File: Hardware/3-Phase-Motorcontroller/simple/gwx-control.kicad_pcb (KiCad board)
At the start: 2 copper layers, 54 x 33 mm, 41 parts, among them IC1 74LS02D, IC2 74123D, J1 MTA07-100, T1 BC850, T2 BC850

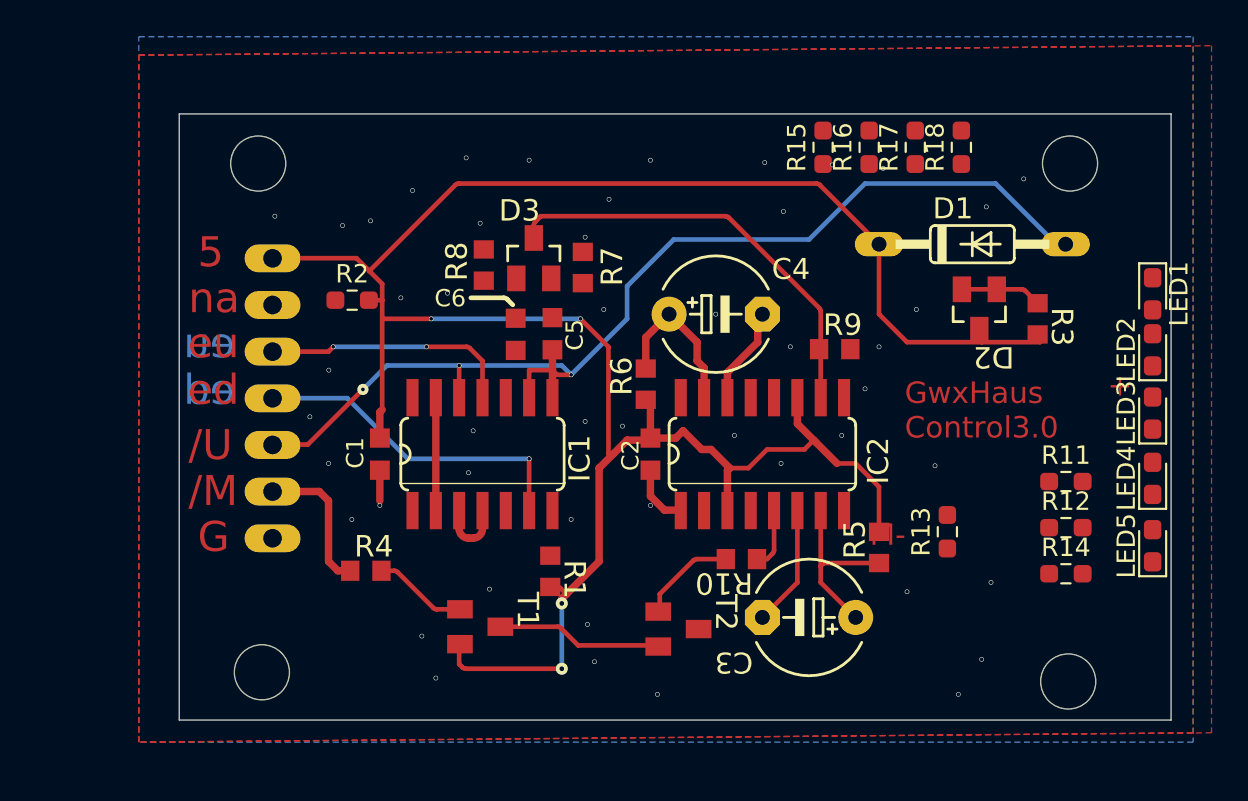
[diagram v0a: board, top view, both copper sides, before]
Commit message: Changed to 2x8 connector
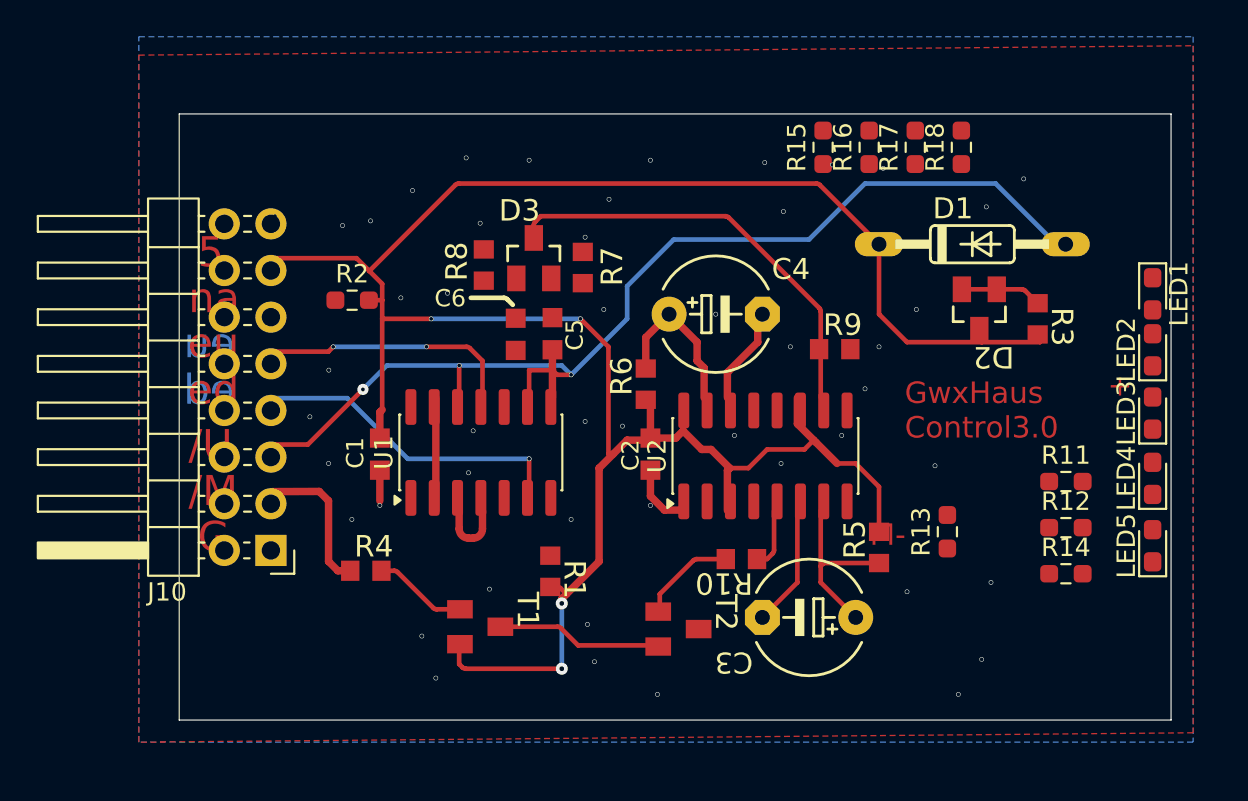
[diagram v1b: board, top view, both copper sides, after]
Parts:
- removed IC1: 74LS02D, SO14
- removed IC2: 74123D, SO16
- removed J1: MTA07-100, 10X07MTA
- removed UNK_HOLE_0: , dummyfp0
- removed UNK_HOLE_1: , dummyfp1
- removed UNK_HOLE_2: , dummyfp2
- removed UNK_HOLE_3: , dummyfp3
- added J10: Conn_02x08_Odd_Even, Connector_PinHeader_2.54mm:PinHeader_2x08_P2.54mm_Horizontal, F.Cu at (126.5, 112.3)
- added U1: 74LS02, Package_SO:SOIC-14_3.9x8.7mm_P1.27mm, F.Cu at (137.9, 106.9)
- added U2: 74LS123, Package_SO:SOIC-16_3.9x9.9mm_P1.27mm, F.Cu at (153.4, 107.1)
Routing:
- net Net-(J10-Pin_7): track 0.00 -> 18.2 mm, vias 0 -> 1
- net //END_DOWN: track 18.2 -> 0.00 mm, vias 1 -> 0
- net Net-(J10-Pin_9): track 0.00 -> 14.4 mm, vias 0 -> 2
- net //END_UP: track 14.4 -> 0.00 mm, vias 3 -> 1
- net Net-(U1-Pad13): track 0.00 -> 6.15 mm
- net Net-(IC1A-I0): track 6.15 -> 0.00 mm
- net Net-(U1-Pad3): track 0.00 -> 3.79 mm
- net Net-(IC1A-I1): track 3.79 -> 0.00 mm
- net VCC: vias 4 -> 5
- net GND: vias 47 -> 46

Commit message: LEDs libs updated
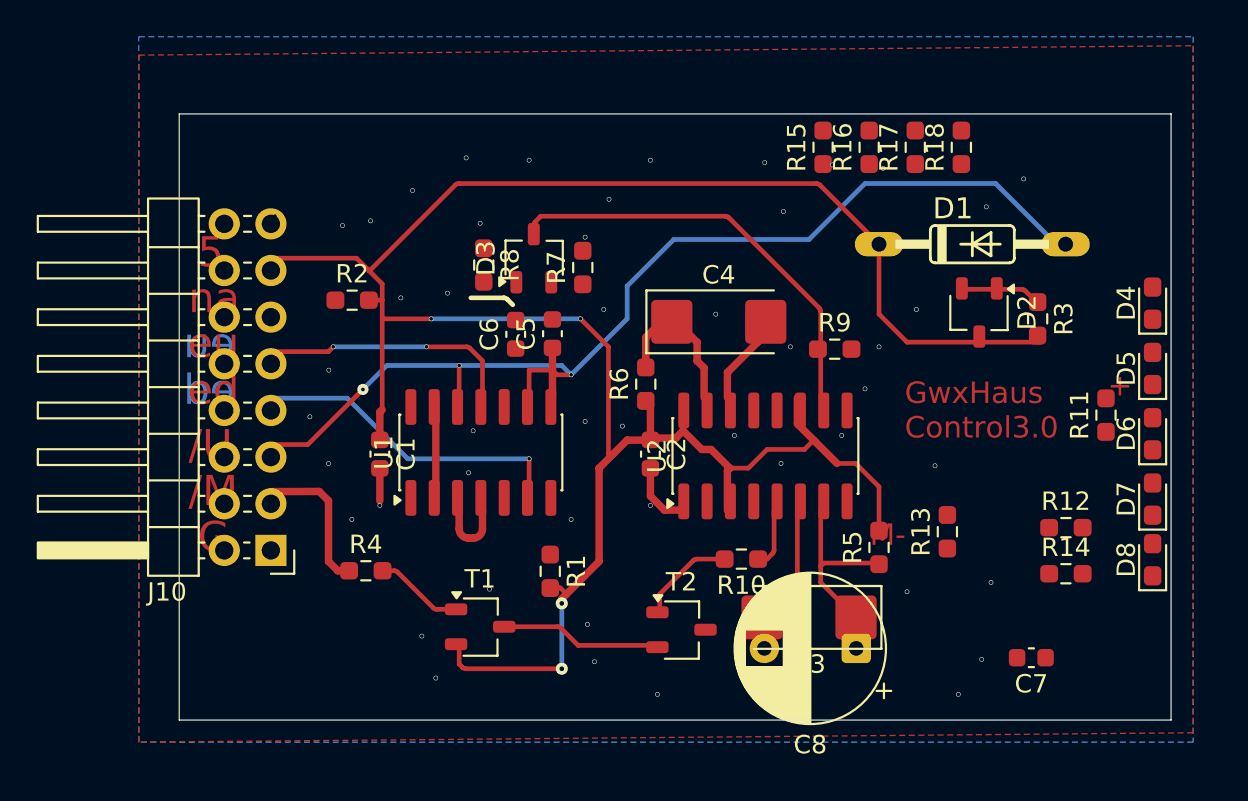
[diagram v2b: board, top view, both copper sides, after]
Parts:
- removed LED1, LED2, LED3, LED4, LED5: LED_ESML0603, LED_SMD:LED_0603_1608Metric_Pad1.05x0.95mm_HandSolder
- added C7: 1µF, Capacitor_SMD:C_0603_1608Metric, F.Cu at (167.9, 118.1)
- added C8: 47µ, Capacitor_THT:CP_Radial_D8.0mm_P5.00mm, F.Cu at (158.4, 117.6)
- added D4: LED_ESML0603, LED_SMD:LED_0603_1608Metric_Pad1.05x0.95mm_HandSolder, F.Cu at (174.5, 98.8)
- added D5: LED_ESML0603, LED_SMD:LED_0603_1608Metric_Pad1.05x0.95mm_HandSolder, F.Cu at (174.5, 102.4)
- added D6: LED_ESML0603, LED_SMD:LED_0603_1608Metric_Pad1.05x0.95mm_HandSolder, F.Cu at (174.5, 105.9)
- added D7: LED_ESML0603, LED_SMD:LED_0603_1608Metric_Pad1.05x0.95mm_HandSolder, F.Cu at (174.5, 109.5)
- added D8: LED_ESML0603, LED_SMD:LED_0603_1608Metric_Pad1.05x0.95mm_HandSolder, F.Cu at (174.5, 112.8)
- C1, C2, C5, C6: footprint C0603K -> Capacitor_SMD:C_0603_1608Metric
- C3: footprint E5-6 -> Capacitor_Tantalum_SMD:CP_EIA-6032-28_Kemet-C_HandSolder
- C4: value CPOL-EUE5-6 -> 47µ; footprint E5-6 -> Capacitor_Tantalum_SMD:CP_EIA-6032-28_Kemet-C_HandSolder
- D2, D3: footprint SOT23 -> Package_TO_SOT_SMD:TSOT-23
- R1, R10, R3, R4, R5, R6, R7, R8, R9: footprint R0603 -> Resistor_SMD:R_0603_1608Metric_Pad0.98x0.95mm_HandSolder
- T1, T2: footprint SOT23-BEC -> Package_TO_SOT_SMD:TSOT-23
- moved R11 4.22 mm to (172.0, 104.9), turned to 90 degrees
- moved C4 0.45 mm to (150.9, 99.8)
- moved T2 0.17 mm to (148.8, 116.6), turned to 0 degrees
- moved D2 0.16 mm to (165.1, 99.3), turned to -90 degrees
- turned D3 to 90 degrees
- turned T1 to 0 degrees
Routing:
- net Net-(T1-PadC): track 9.02 -> 0.00 mm
- net (no net): track 0.00 -> 9.02 mm

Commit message: PCB shrinked
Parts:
- removed D1: 1N4148, DO35-10
- removed R18: 4k7, Resistor_SMD:R_0603_1608Metric_Pad0.98x0.95mm_HandSolder
- added C10: 100n, Capacitor_SMD:C_0603_1608Metric, F.Cu at (131.0, 118.4)
- added C9: 100n, Capacitor_SMD:C_0603_1608Metric, F.Cu at (131.0, 115.9)
- moved C7 44.4 mm to (131.1, 93.2), turned to 0 degrees
- moved R2 36.9 mm to (166.4, 108.7), turned to -90 degrees
- moved R16 32.8 mm to (129.0, 103.6), turned to -90 degrees
- moved R17 29.4 mm to (133.9, 100.1)
- moved R3 29.2 mm to (140.1, 92.0)
- moved D2 29.2 mm to (136.9, 91.7)
- moved R13 28.8 mm to (136.9, 99.8), turned to 180 degrees
- moved R15 28.3 mm to (129.5, 98.8)
- moved R1 24.7 mm to (166.4, 112.2)
- moved R12 10.2 mm to (166.4, 101.4), turned to -90 degrees
- moved R11 9.33 mm to (166.4, 97.4), turned to -90 degrees
- moved R14 8.91 mm to (166.4, 105.3), turned to -90 degrees
- moved D6 5.26 mm to (169.4, 104.5)
- moved D7 5.26 mm to (169.4, 108.1)
- moved D4 5.26 mm to (169.4, 97.4)
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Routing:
- net //UP: track 64.1 -> 52.3 mm, vias 3 -> 4
- net VCC: track 128.1 -> 118.1 mm
- net Net-(J10-Pin_7): vias 1 -> 2
- net GND: vias 46 -> 44
- net //END_UP: vias 1 -> 0
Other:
- board size 54 x 33 mm -> 49 x 32 mm
